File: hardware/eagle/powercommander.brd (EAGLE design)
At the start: 100 x 85 mm, 39 parts, among them IC1 ULN2803SO18-1, IC2 7805TV, IC3 MCP2551SOIC8, K1 G5NB, K2 G5NB, K3 G5NB, K4 G5NB, K5 G5NB, K6 G5NB, K7 G5NB, K8 G5NB, X2 3KLEMME, X3 2KLEMME, X4 2KLEMME, X5 2KLEMME, X6 2KLEMME

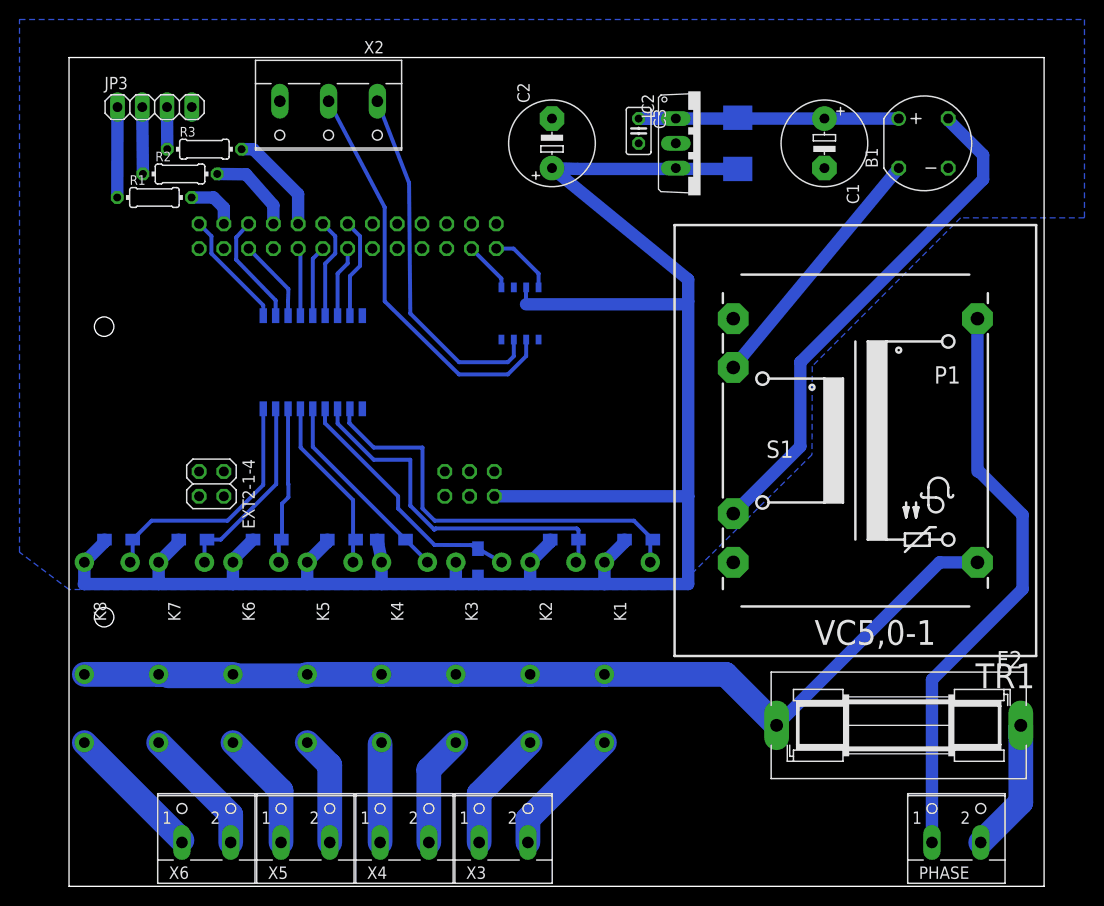
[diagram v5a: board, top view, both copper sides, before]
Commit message: klemme angepasst
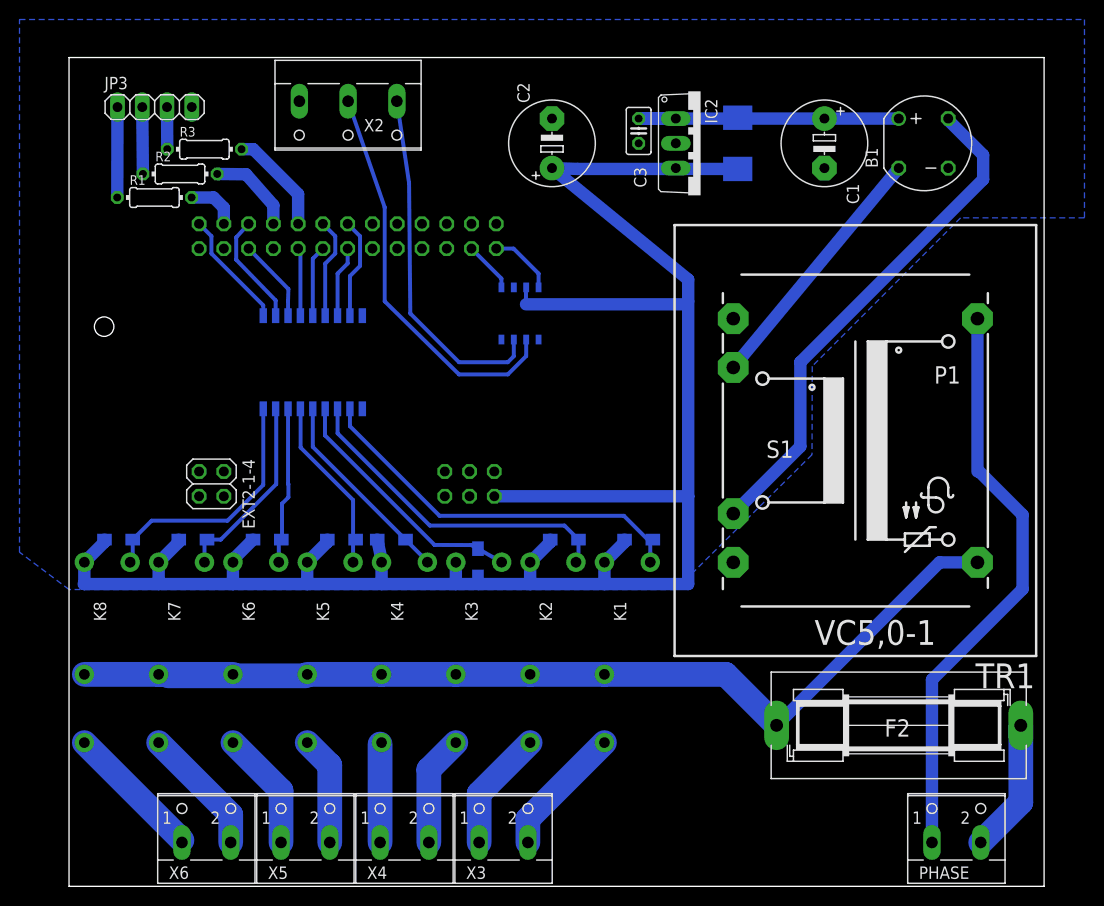
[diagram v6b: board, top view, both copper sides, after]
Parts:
- D1, D2, D3, D4, D5, D6, D7, D8: value (none) -> 1N4148
- D9: value (none) -> 1N4001
- EXT2-1-4: value (none) -> 2x2
- EXT2-21-26: value (none) -> 3x2
- TR1: value (none) -> VC5,0-1
- moved X2 2.00 mm to (28.6, 80.5)
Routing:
- net N$20: track 43.7 -> 39.9 mm
- net N$10: track 37.0 -> 34.2 mm
- net N$6: track 42.0 -> 41.2 mm
- net N$2: track 37.0 -> 36.5 mm

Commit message: new boardlayout +  pwm  für relay added
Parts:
- C1: value 10µF -> 2000µF
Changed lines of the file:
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@@
 <attribute name="OC_FARNELL" value="unknown" x="-33.02" y="0" size="1.778" layer="27" rot="R270" display="off"/>
 </element>
-<element name="C1" library="rcl" package="E5-8,5" value="10µF" x="77.47" y="76.2" rot="R270"/>
+<element name="C1" library="rcl" package="E5-8,5" value="2000µF" x="77.47" y="76.2" rot="R270"/>
 <element name="C2" library="rcl" package="E5-8,5" value="10µF" x="49.53" y="76.2" rot="R90"/>
 <element name="C3" library="rcl" package="C025-025X050" value="10nF" x="58.42" y="77.47" smashed="yes" rot="R270">
